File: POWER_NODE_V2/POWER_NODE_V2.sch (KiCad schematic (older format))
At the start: 0 parts

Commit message: WIP
making good progress
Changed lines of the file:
@@
 $EndSheet
 $Sheet
-S 2600 900  2200 4750
+S 2600 900  2200 5350
 U 594B2261
 F0 "RM57 Core" 60
@@
 F4 "I2C2_SCL" I L 5650 1550 60
 F5 "I2C2_SDA" I L 5650 1450 60
+F6 "ONE_WIRE_BATT_1_3" O R 7400 1050 61
+F7 "ONE_WIRE_BATT_4_6" O R 7400 1150 61
+F8 "ONE_WIRE_BATT_7_9" O R 7400 1250 61
+F9 "ONE_WIRE_BATT_10_12" O R 7400 1350 61
+F10 "ONE_WIRE_BATT_13_15" O R 7400 1450 61
+F11 "ONE_WIRE_BATT_16_18" O R 7400 1550 61
+F12 "ONE_WIRE_BATT_BMS" O R 7400 1650 61
 $EndSheet
 $Sheet
@@
 F10 "BMS_FAULT" O L 5650 3900 60
 F11 "BMS_ALERT" O L 5650 4000 60
+F12 "1-Wire" I R 7650 3300 61
 $EndSheet
 $Sheet
-S 5650 4700 2050 950
+S 5650 4700 2000 1500
 U 594B22A6
 F0 "Charger Interface" 60
 F1 "Charger Interface.sch" 60
+F2 "CHR_RLY" I L 5650 4850 60
+F3 "CHG_I" O L 5650 5150 60
+F4 "BATT_VOLT" O L 5650 5350 60
+F5 "CHG_VOLT" O L 5650 4950 60
+F6 "BATT_I" O L 5650 5550 60
+F7 "CHG_I_REF" O L 5650 5050 60
+F8 "BATT_I_REF" O L 5650 5450 60
 $EndSheet
 Wire Wire Line
@@
 Wire Wire Line
 	5650 1550 4800 1550
+Wire Wire Line
+	7400 1650 8200 1650
+Wire Wire Line
+	8200 1650 8200 3300
+Wire Wire Line
+	8200 3300 7650 3300
 $EndSCHEMATC

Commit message: Power Node V2 WIP
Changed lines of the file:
@@
 F0 "RM57 Core" 60
 F1 "RM57 Core.sch" 60
-F2 "CHG_RLY" O R 4800 4950 60
-F3 "CHG_CURRENT" I R 4800 5050 60
-F4 "CHG_VOLT" I R 4800 5350 60
-F5 "BATT_VOLT" I R 4800 5250 60
-F6 "DC_WATCHDOG" O R 4800 2500 60
-F7 "BMS_SCK" O R 4800 3200 60
-F8 "BMS_MOSI" O R 4800 3300 60
-F9 "BMS_NCS" O R 4800 3500 60
-F10 "BMS_MISO" O R 4800 3400 60
-F11 "BMS_DRDY" I R 4800 3700 60
-F12 "BMS_COMMS_EN" O R 4800 3600 60
-F13 "BMS_CONV" O R 4800 3800 60
-F14 "RM57_I2C1_SDA" O R 4800 1100 60
-F15 "RM57_I2C1_SCL" O R 4800 1200 60
-F16 "RM57_I2C2_SDA" O R 4800 1450 60
-F17 "RM57_I2C2_SDC" O R 4800 1550 60
-F18 "BMS_FAN" O R 4800 4150 60
-F19 "BMS_FAULT" I R 4800 3900 60
-F20 "BMS_ALERT" I R 4800 4000 60
+F2 "CHG_RLY" O R 4800 4850 60
+F3 "CHG_VOLT" I R 4800 4950 60
+F4 "BATT_VOLT" I R 4800 5350 60
+F5 "DC_WATCHDOG" O R 4800 2500 60
+F6 "BMS_SCK" O R 4800 3200 60
+F7 "BMS_MOSI" O R 4800 3300 60
+F8 "BMS_NCS" O R 4800 3500 60
+F9 "BMS_MISO" O R 4800 3400 60
+F10 "BMS_DRDY" I R 4800 3700 60
+F11 "BMS_COMMS_EN" O R 4800 3600 60
+F12 "BMS_CONV" O R 4800 3800 60
+F13 "RM57_I2C1_SDA" O R 4800 1100 60
+F14 "RM57_I2C1_SCL" O R 4800 1200 60
+F15 "RM57_I2C2_SDA" O R 4800 1450 60
+F16 "RM57_I2C2_SCL" O R 4800 1550 60
+F17 "BMS_FAN" O R 4800 4150 60
+F18 "BMS_FAULT" I R 4800 3900 60
+F19 "BMS_ALERT" I R 4800 4000 60
+F20 "CHG_I_REF" I R 4800 5050 60
+F21 "CHG_I" I R 4800 5150 60
+F22 "BATT_I_REF" I R 4800 5450 60
+F23 "BATT_I" I R 4800 5550 60
 $EndSheet
 $Sheet
@@
 $EndSheet
 $Sheet
-S 5650 3050 2000 1400
+S 5650 3050 1750 1350
 U 594B229B
 F0 "BMS Interface" 60
@@
 F10 "BMS_FAULT" O L 5650 3900 60
 F11 "BMS_ALERT" O L 5650 4000 60
-F12 "1-Wire" I R 7650 3300 61
+F12 "1-Wire" I R 7400 3300 61
 $EndSheet
 $Sheet
-S 5650 4700 2000 1500
+S 5650 4700 1750 1100
 U 594B22A6
 F0 "Charger Interface" 60
@@
 	7400 1650 8200 1650
 Wire Wire Line
-	8200 1650 8200 3300
+	8200 3300 8200 1650
 Wire Wire Line
-	8200 3300 7650 3300
+	7400 3300 8200 3300
+Wire Wire Line
+	4800 4850 5650 4850
+Wire Wire Line
+	5650 4950 4800 4950
+Wire Wire Line
+	4800 5050 5650 5050
+Wire Wire Line
+	5650 5150 4800 5150
+Wire Wire Line
+	4800 5350 5650 5350
+Wire Wire Line
+	5650 5450 4800 5450
+Wire Wire Line
+	4800 5550 5650 5550
 $EndSCHEMATC

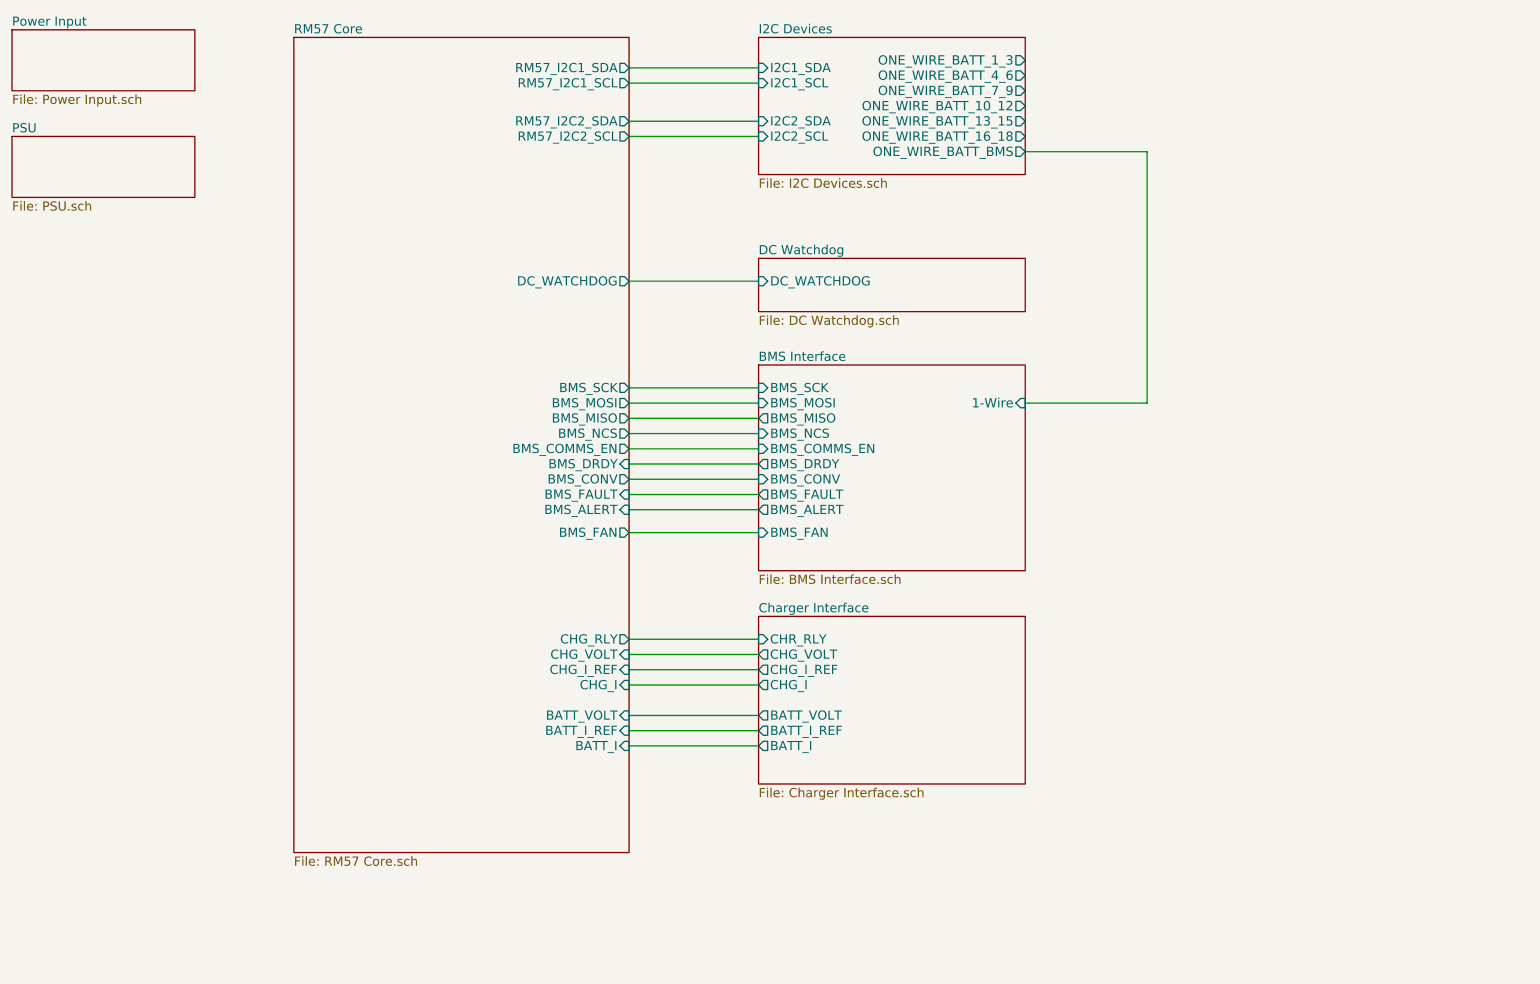
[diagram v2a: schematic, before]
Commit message: Schematic for Power Node V2 mostly done - mostly need connectors
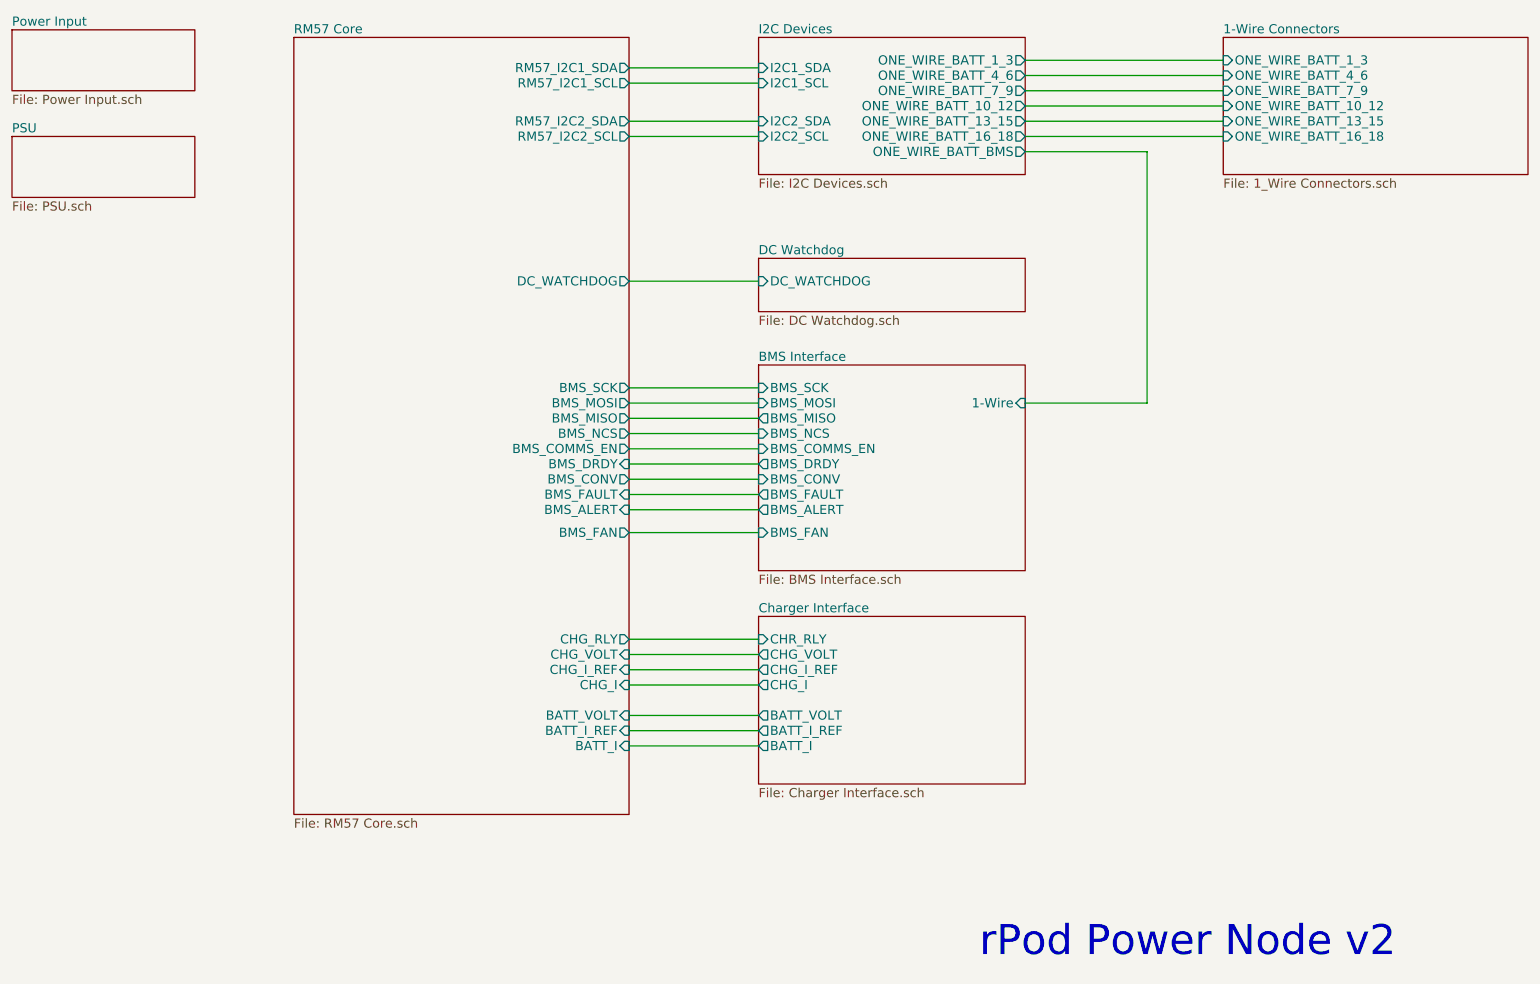
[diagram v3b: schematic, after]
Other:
- note added: "rPod Power Node v2"
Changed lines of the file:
@@
 $Descr A4 11693 8268
 encoding utf-8
-Sheet 1 8
+Sheet 1 9
 Title ""
 Date ""
@@
 $EndSheet
 $Sheet
-S 2600 900  2200 5350
+S 2600 900  2200 5100
 U 594B2261
 F0 "RM57 Core" 60
@@
 	7400 1650 8200 1650
 Wire Wire Line
-	8200 3300 8200 1650
+	8200 1650 8200 3300
 Wire Wire Line
-	7400 3300 8200 3300
+	8200 3300 7400 3300
 Wire Wire Line
 	4800 4850 5650 4850
@@
 Wire Wire Line
 	4800 5550 5650 5550
+$Sheet
+S 8700 900  2000 900
+U 5952325B
+F0 "1-Wire Connectors" 60
+F1 "1_Wire Connectors.sch" 60
+F2 "ONE_WIRE_BATT_1_3" I L 8700 1050 60
+F3 "ONE_WIRE_BATT_4_6" I L 8700 1150 60
+F4 "ONE_WIRE_BATT_7_9" I L 8700 1250 60
+F5 "ONE_WIRE_BATT_10_12" I L 8700 1350 60
+F6 "ONE_WIRE_BATT_13_15" I L 8700 1450 60
+F7 "ONE_WIRE_BATT_16_18" I L 8700 1550 60
+$EndSheet
+Wire Wire Line
+	7400 1050 8700 1050
+Wire Wire Line
+	8700 1150 7400 1150
+Wire Wire Line
+	7400 1250 8700 1250
+Wire Wire Line
+	7400 1350 8700 1350
+Wire Wire Line
+	7400 1450 8700 1450
+Wire Wire Line
+	8700 1550 7400 1550
+Text Notes 7100 6950 0    197  ~ 0
+rPod Power Node v2
 $EndSCHEMATC

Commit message: Added tooling holes & fiducial marks
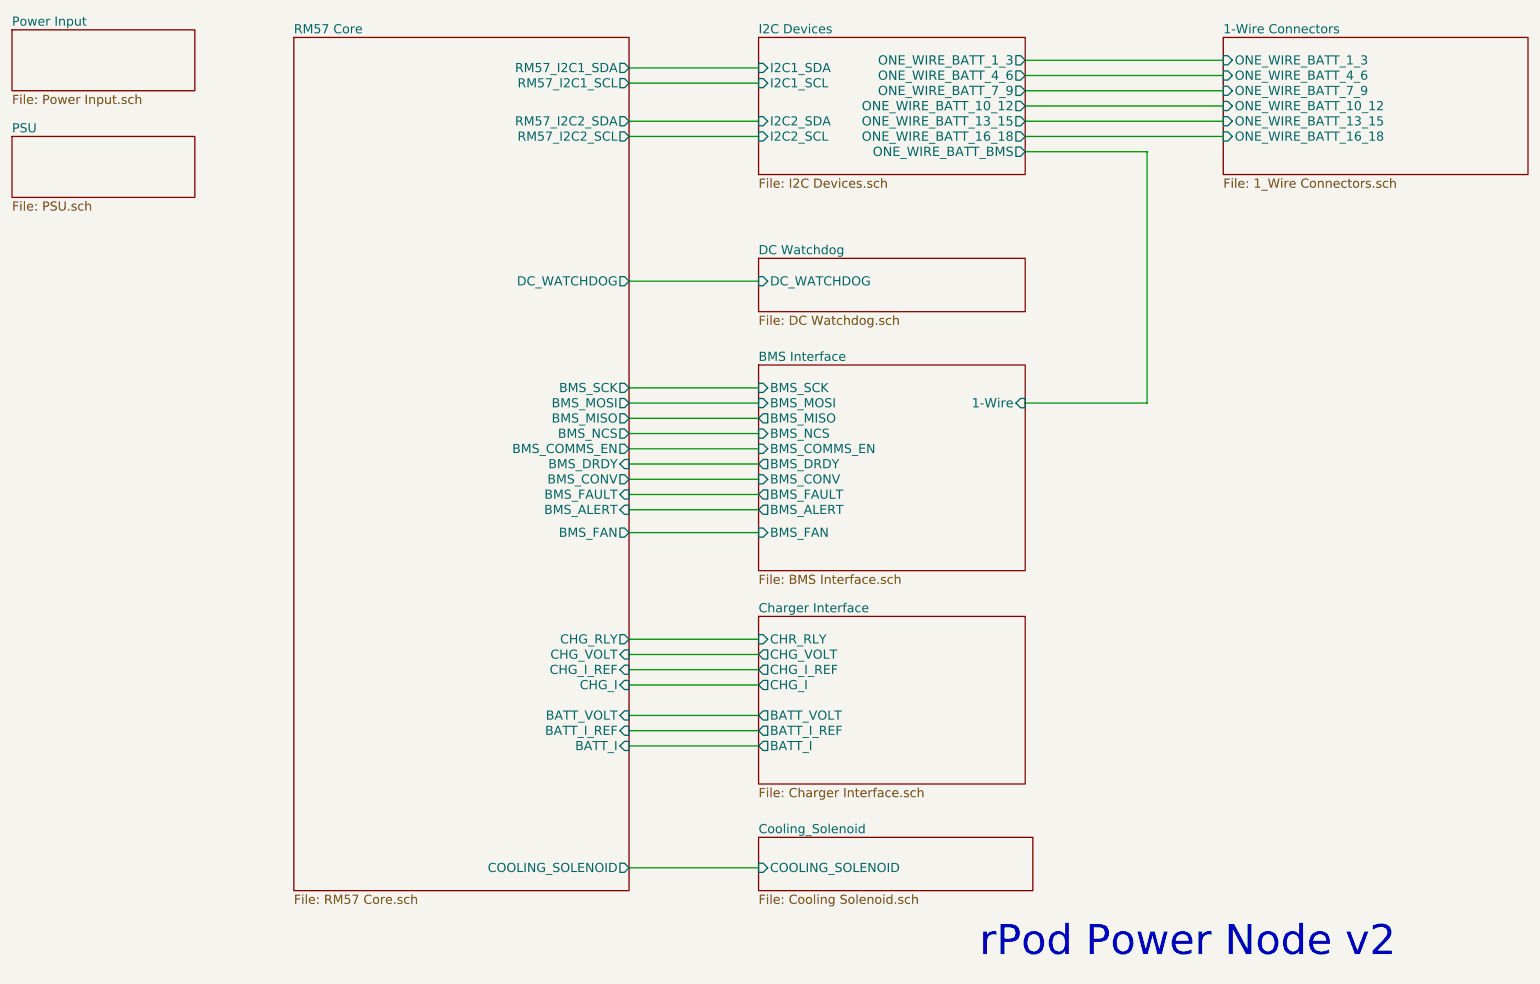
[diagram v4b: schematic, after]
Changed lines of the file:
@@
 EESchema Schematic File Version 2
+LIBS:POWER_NODE_V2-rescue
 LIBS:power
 LIBS:device
@@
 $Descr A4 11693 8268
 encoding utf-8
-Sheet 1 9
+Sheet 1 10
 Title ""
 Date ""
@@
 $EndSheet
 $Sheet
-S 2600 900  2200 5100
+S 2600 900  2200 5600
 U 594B2261
 F0 "RM57 Core" 60
@@
 F22 "BATT_I_REF" I R 4800 5450 60
 F23 "BATT_I" I R 4800 5550 60
+F24 "COOLING_SOLENOID" O R 4800 6350 60
 $EndSheet
 $Sheet
@@
 Text Notes 7100 6950 0    197  ~ 0
 rPod Power Node v2
+$Sheet
+S 5650 6150 1800 350
+U 5965B6EF
+F0 "Cooling_Solenoid" 60
+F1 "Cooling Solenoid.sch" 60
+F2 "COOLING_SOLENOID" I L 5650 6350 60
+$EndSheet
+Wire Wire Line
+	4800 6350 5650 6350
 $EndSCHEMATC
